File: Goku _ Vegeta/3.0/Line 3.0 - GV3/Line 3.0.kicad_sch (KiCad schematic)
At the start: 58 parts

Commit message: Line 3.0 schematic
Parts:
- removed D?: 1N5408, Diode_THT:D_DO-201AD_P15.24mm_Horizontal, symbol Diode:1N5408
- removed U?: DC-DC_Multi-output_Buck_Converter_(3.3V/5V/9V/12V), symbol DC-DC Multi-output Buck Converter (3:DC-DC_Multi-output_Buck_Converter_(3.3V{sl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
- added C1, C6: 100uF, Capacitor_THT:CP_Radial_D10.0mm_P5.00mm, symbol Device:C_Polarized_Small
- added C10: 0.1uF, Capacitor_SMD:C_0805_2012Metric, symbol Device:C_Polarized_Small
- added C2, C5: 1uF, Capacitor_SMD:C_0805_2012Metric, symbol Device:C_Polarized_Small
- added C3, C4: 560uF, Capacitor_THT:CP_Radial_D18.0mm_P7.50mm, symbol Device:C_Polarized
- added C7: 22uF, Capacitor_SMD:C_0805_2012Metric, symbol Device:C_Polarized_Small
- added C8: 10uF, Capacitor_SMD:C_0805_2012Metric, symbol Device:C_Polarized_Small
- added C9: 3.3nF, Capacitor_SMD:C_0805_2012Metric, symbol Device:C_Polarized_Small
- added D1: SS510, Diode_SMD:D_SOD-128, symbol Device:D_Schottky
- added D2, D5: STTH2002G-TR, Package_TO_SOT_SMD:TO-263-2, symbol Diode:STTH2002G
- added J1: Solenoid, TerminalBlock:TerminalBlock_bornier-2_P5.08mm, symbol Connector:Screw_Terminal_01x02
- added J11: Kicker Voltmeter, TerminalBlock:TerminalBlock_bornier-2_P5.08mm, symbol Connector:Screw_Terminal_01x02
- added J3: Motor 1, Connector_PinSocket_2.54mm:PinSocket_1x06_P2.54mm_Vertical, symbol Connector:Conn_01x06_Pin
- added J4: Motor 3, Connector_PinSocket_2.54mm:PinSocket_1x06_P2.54mm_Vertical, symbol Connector:Conn_01x06_Pin
- added J5: Motor 2, Connector_PinSocket_2.54mm:PinSocket_1x06_P2.54mm_Vertical, symbol Connector:Conn_01x06_Pin
- added J6: Motor 4, Connector_PinSocket_2.54mm:PinSocket_1x06_P2.54mm_Vertical, symbol Connector:Conn_01x06_Pin
- added L1: 56uH, symbol Device:L
- added L2: 2.2uH, symbol Device:L
- added Q2: BSC040N10NS5, Package_TO_SOT_SMD:TDSON-8-1, symbol Transistor_FET:BSC040N10NS5
- added R1: 2K94, Resistor_SMD:R_0805_2012Metric, symbol Device:R_Small
- added R2: 57K, Resistor_SMD:R_0805_2012Metric, symbol Device:R_Small
- added R29: CT6EP103, symbol POT_CT-6EP_NDC:CT6EP103
- added R3: 1K5, Resistor_SMD:R_0805_2012Metric, symbol Device:R_Small
- added R30: 100K, Resistor_SMD:R_0805_2012Metric, symbol Device:R_Small
- added U1: LM2587S-ADJ, LM2587S-ADJ:VREG_TPS79625KTTR, symbol LM2587S-ADJ:LM2587S-ADJ
- added U10: TPS62132, Package_DFN_QFN:VQFN-16-1EP_3x3mm_P0.5mm_EP1.68x1.68mm_ThermalVias, symbol Regulator_Switching:TPS62132
- added U2, U3, U4, U5: TB67H420FTG Dual/Single Motor Driver Carrier, LM2587S-ADJ:VREG_TPS79625KTTR, symbol TB67H420FTG Dual_Single Motor Driver Carrier:LM2587S-ADJ
- A1, A10, A11, A12, A2, A3, A4, A5, A6, A7, A8, A9: renamed from A?; footprint XDCR_ALS-PT19-315C/L177/TR8 -> ALS-PT19-315C_L177_TR8:XDCR_ALS-PT19-315C_L177_TR8
- J7: renamed from J?; footprint (none) -> Connector_AMASS:AMASS_XT60-F_1x02_P7.20mm_Vertical
- J8: renamed from J?; footprint (none) -> Connector_JST:JST_XH_B4B-XH-AM_1x04_P2.50mm_Vertical
- LED1, LED10, LED11, LED12, LED2, LED3, LED4, LED5, LED6, LED7, LED8, LED9: renamed from LED?; footprint LED_J2835_CRW -> JB2835AWT-W-U30GA0000-N0000001:LED_J2835_CRW
- U9: renamed from U?; footprint MODULE_DEV-16771 -> DEV-16771:MODULE_DEV-16771
- gave numbers to parts that had none: 29
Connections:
- net +15V: now also J7.1 (Pin_1), C10.1, C6.1, C8.1, D2.3 (A), L1.1, U1.5 (VIN), U10.10 (AVIN), U10.11 (PVIN), U10.12 (PVIN), U10.13 (EN), U2.14 (VIN), U3.14 (VIN), U4.14 (VIN), U5.14 (VIN); no longer U6.2 (IN+)
- net +3V3: now also C7.1, J3.4 (Pin_4), J4.4 (Pin_4), J5.4 (Pin_4), J6.4 (Pin_4), L2.2, R30.2, U10.14 (VOS)
- net 10: now also U4.4 (INA1)
- net 2: now also C5.1
- net 28: now also J4.5 (Pin_5)
- net 29: now also J4.6 (Pin_6)
- net 3: now also U3.6 (PWMA)
- net 30: now also J3.5 (Pin_5)
- net 31: now also J3.6 (Pin_6)
- net 33: now also U4.5 (INA2)
- net 34: now also J5.5 (Pin_5)
- net 35: now also J5.6 (Pin_6)
- net 36: now also U3.5 (INA2)
- net 37: now also U3.4 (INA1)
- net 38: now also U5.5 (INA2)
- net 39: now also U5.4 (INA1)
- net 4: now also U4.6 (PWMA)
- net 40: now also U2.5 (INA2)
- net 41: now also U2.4 (INA1)
- net 5: now also U2.6 (PWMA)
- net 6: now also U5.6 (PWMA)
- net 7: now also J6.5 (Pin_5)
- net 8: now also J6.6 (Pin_6)
- net 9: now also Q2.4 (G)
- net GND: now also C1.2, C10.2, C2.2, C3.2, C4.2, C5.2, C6.2, C7.2, C8.2, C9.1, J11.2 (Pin_2), J3.3 (Pin_3), J4.3 (Pin_3), J5.3 (Pin_3), J6.3 (Pin_3), Q2.1 (S), Q2.2 (S), Q2.3 (S), R3.2, U1.3 (GND), U1.6 (GND__1), U10.15 (PGND), U10.16 (PGND), U10.17 (EP), U10.5 (FB), U10.6 (AGND), U10.7 (FSW), U10.8 (DEF), U2.15 (GND), U2.2 (GND), U3.15 (GND), U3.2 (GND), U4.15 (GND), U4.2 (GND), U5.15 (GND), U5.2 (GND)
- new net: D2.2 (K), U6.2 (IN+)
- new net: R1.1, U1.1 (COMP)
- new net: C2.1, R1.2
- new net: C9.2, U10.9 (SS/TR)
- new net: J3.1 (Pin_1), U3.16 (B+), U3.17 (B-)
- new net: J3.2 (Pin_2), U3.18 (A-), U3.19 (A+)
- new net: C1.1, C3.1, C4.1, D1.1 (K), D5.3 (A), J1.1 (Pin_1), J11.1 (Pin_1), R2.1
- new net: J5.1 (Pin_1), U4.16 (B+), U4.17 (B-)
- new net: J5.2 (Pin_2), U4.18 (A-), U4.19 (A+)
- new net: D5.2 (K), J1.2 (Pin_2), Q2.5 (D)
- new net: U4.20 (VCC), U4.21 (VCC), U4.23 (HBMODE)
- new net: J4.1 (Pin_1), U2.16 (B+), U2.17 (B-)
- new net: J4.2 (Pin_2), U2.18 (A-), U2.19 (A+)
- new net: U2.20 (VCC), U2.21 (VCC), U2.23 (HBMODE)
- new net: R2.2, R29.3
- new net: L2.1, U10.1 (SW), U10.2 (SW), U10.3 (SW)
- new net: R30.1, U10.4 (PG)
- new net: J6.1 (Pin_1), U5.16 (B+), U5.17 (B-)
- new net: J6.2 (Pin_2), U5.18 (A-), U5.19 (A+)
- new net: R29.1, R29.2, R3.1, U1.2 (FB)
- new net: D1.2 (A), L1.2, U1.4 (SW)
- new net: U3.20 (VCC), U3.21 (VCC), U3.23 (HBMODE)
- new net: U5.20 (VCC), U5.21 (VCC), U5.23 (HBMODE)
- no-connect marks 14 -> 54
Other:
- note added: "Boost Circuit"
- note added: "KICKER CHARGE PUMP"
- note added: "LEDs & Photo Transistors"
- note added: "LINE SENSORS"
- note added: "MOTOR DRIVERS"
- note added: "NEXT STEPS: - organise config to warning - urgent signals MAYBE: - integrate power supply circuits"
- note added: "NOTES TO SELF"
- note added: "Urgent Line Sensors - Conditional Poll"
- note added: "Warning Line Sensors - Constant Poll"
- note removed: "LEDs & Photo T"
- company: (none) -> Team Silverback
- title: (none) -> LINE 3.0 PCB
- moved on the sheet: A1, A10, A11, A12, A2, A3, A4, A5, A6, A7, A8, A9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

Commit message: Line 3.0 SCH 1st draft done + started working on SCH for main 3.0
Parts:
- removed U6: DC-DC_Buck_Converter_7-24V_to_5V_4A, 2.3 PCBs:DC-DC_Buck_Converter_7-24V_to_5V_4A, symbol DC-DC Buck Converter 7-24V to 5V 4A:DC-DC_Buck_Converter_7-24V_to_5V_4A
- added C15: 10uF, Capacitor_SMD:C_0805_2012Metric, symbol Device:C_Polarized_Small
- added C16: 0.1uF, Capacitor_SMD:C_0805_2012Metric, symbol Device:C_Polarized_Small
- added C17: 3.3nF, Capacitor_SMD:C_0805_2012Metric, symbol Device:C_Polarized_Small
- added C18: 22uF, Capacitor_SMD:C_0805_2012Metric, symbol Device:C_Polarized_Small
- added D3: STTH2002G-TR, Package_TO_SOT_SMD:TO-263-2, symbol Diode:STTH2002G
- added L4: 2.2uH, symbol Device:L
- added R32: 100K, Resistor_SMD:R_0805_2012Metric, symbol Device:R_Small
- added U11: TPS62133, Package_DFN_QFN:VQFN-16-1EP_3x3mm_P0.5mm_EP1.68x1.68mm_ThermalVias, symbol Regulator_Switching:TPS62133
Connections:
- net INT is gone; now on net 32: J8.1 (Pin_1)
- net +15V: now also D3.3 (A); no longer C10.1, C8.1, D2.3 (A), U10.10 (AVIN), U10.11 (PVIN), U10.12 (PVIN), U10.13 (EN)
- net +5V: now also C18.1, L4.2, R32.2, U11.14 (VOS)
- net GND: now also C18.2, U11.15 (PGND), U11.16 (PGND), U11.17 (EP), U11.5 (FB)
- net at D2.2 (K): now also C15.1, C16.1, U11.10 (AVIN), U11.11 (PVIN), U11.12 (PVIN), U11.13 (EN)
- new net: C10.1, C8.1, D3.2 (K), U10.10 (AVIN), U10.11 (PVIN), U10.12 (PVIN), U10.13 (EN)
- new net: C15.2, C16.2, C17.1, U11.6 (AGND), U11.7 (FSW), U11.8 (DEF)
- new net: L4.1, U11.1 (SW), U11.2 (SW), U11.3 (SW)
- new net: R32.1, U11.4 (PG)
- new net: C17.2, U11.9 (SS/TR)
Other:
- note added: "3V3 POWER RAIL - LEDs and Phototransistors"
- note added: "5V POWER RAIL - Microcontroller"
- note added: "Kick Circuit"
- note added: "NEXT STEPS: add footprint for motor drivers finish adding in footprints for inductors etc. MAYBE:"
- note removed: "LEDs & Photo Transistors"
- note removed: "MCU PWR"
- note removed: "NEXT STEPS: - organise config to warning - urgent signals MAYBE: - integrate power supply circuits"
- moved on the sheet: C1, C10, C2, C3, C4, C5, C6, C7, C8, C9, D1, D5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

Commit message: sumonyx code
need to get
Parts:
- removed L4: 2.2uH, symbol Device:L
- added A13, A14, A15, A16: ALS-PT19-315C/L177/TR8, ALS-PT19-315C_L177_TR8:XDCR_ALS-PT19-315C_L177_TR8, symbol ALS-PT19-315C_L177_TR8:ALS-PT19-315C/L177/TR8
- added L3: 2.2uH, Inductor_SMD:L_Bourns_SRR1260, symbol Device:L
- added LED13, LED14, LED15, LED16: JB2835AWT-W-U30GA0000-N0000001, JB2835AWT-W-U30GA0000-N0000001:LED_J2835_CRW, symbol JB2835AWT-W-U30GA0000-N0000001:JB2835AWT-W-U30GA0000-N0000001
- added R31, R34, R36, R38: 12R, Resistor_SMD:R_0805_2012Metric, symbol Device:R_Small_US
- added R33, R35, R37, R39: 10K, Resistor_SMD:R_0805_2012Metric, symbol Device:R_Small_US
- L1, L2: footprint (none) -> Inductor_SMD:L_Bourns_SRR1260
- R29: footprint (none) -> POT_CT-6EP_NDC:POT_CT-6EP_NDC
- U2, U3, U4, U5: footprint LM2587S-ADJ:VREG_TPS79625KTTR -> TB67H420FTG Dual_Single Motor Driver Carrier:TB67H420FTG DualSingle Motor Driver Carrier
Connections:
- net SEN10 is gone; now on net SEN1: A10.2, R24.2
- net +3V3: now also A13.1, A14.1, A15.1, A16.1, R31.1, R34.1, R36.1, R38.1
- net +5V: now also L3.2
- net 14: no longer A6.2, R16.2
- net 15: no longer A5.2, R14.2
- net 16: no longer A4.2, R12.2
- net 17: no longer A3.2, R10.2
- net 20: no longer A7.2, R18.2
- net 21: no longer A8.2, R20.2
- net 22: no longer A9.2, R22.2
- net 23: no longer A11.2, R26.2
- net 24: no longer A2.2, R8.2
- net 25: no longer A12.2, R28.2
- net GND: now also R33.1, R35.1, R37.1, R39.1
- net MSFTDRN: now also LED13.1, LED14.1, LED15.1, LED16.1
- net SEN1: now also A11.2, A12.2, A2.2, A3.2, A4.2, A5.2, A6.2, A7.2, A8.2, A9.2, R10.2, R12.2, R14.2, R16.2, R18.2, R20.2, R22.2, R26.2, R28.2, R8.2, A13.2, A14.2, A15.2, A16.2, R33.2, R35.2, R37.2, R39.2
- net at U11.1 (SW), U11.2 (SW), U11.3 (SW): now also L3.1
- new net: LED16.2, R38.2
- new net: LED14.2, R34.2
- new net: LED15.2, R36.2
- new net: LED13.2, R31.2
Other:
- note added: "2nd Warning Line Sensors - Conditonal Poll"
- moved on the sheet: A1, LED1, R4, R5

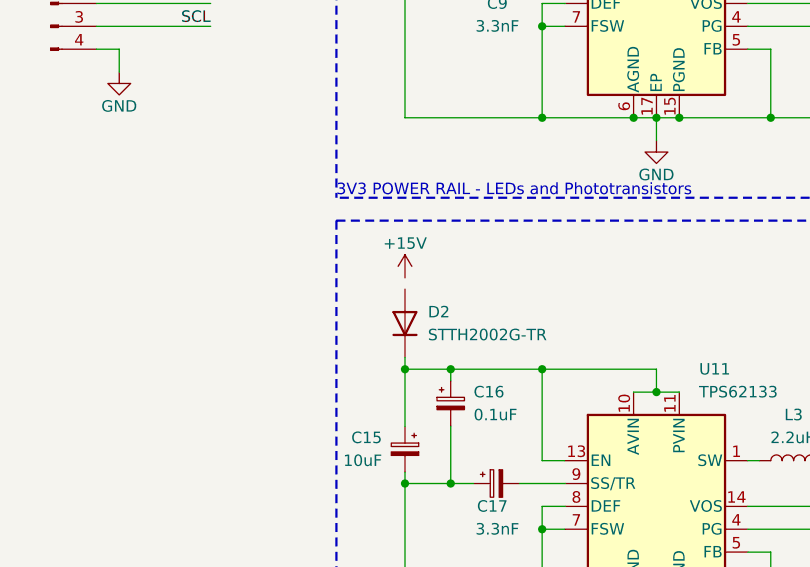
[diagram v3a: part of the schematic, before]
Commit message: Started 3.1 PCBs
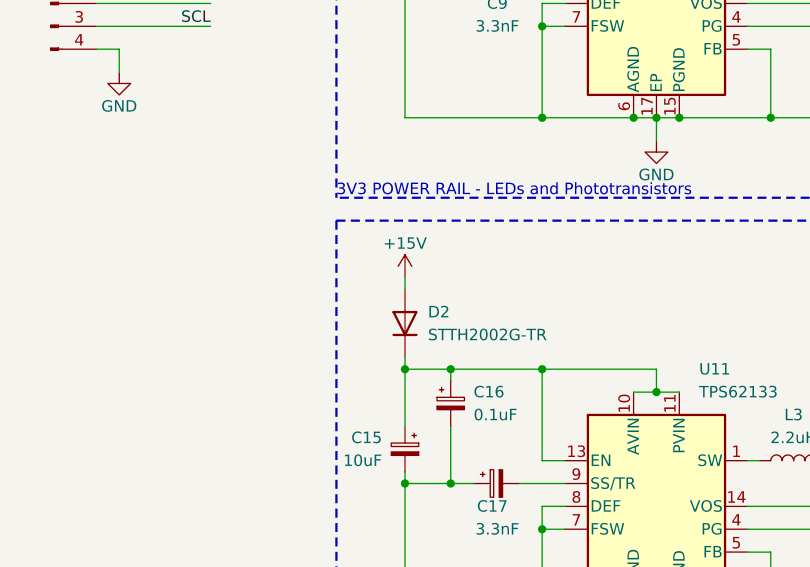
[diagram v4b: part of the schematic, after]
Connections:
- net +15V: now also D2.3 (A)
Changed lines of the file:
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@@
+    (stroke (width 0) (type default))
+  )
+  (wire (pts (xy 74.93 166.37) (xy 74.93 167.64))
     (stroke (width 0) (type default))
   )
